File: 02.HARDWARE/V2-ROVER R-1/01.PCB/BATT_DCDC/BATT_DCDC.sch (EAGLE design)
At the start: 61 parts, among them J1 DF40C-20DP-0.4V_51_, K1 FLEX11, Q1 NVTFS9D6P04M8LTAG, Q2 2N7002PW, Q5 2N7002PW, U1 MCP6071T-E/OT, U3 TPS55330RTET, U7 MCP6071T-E/OT

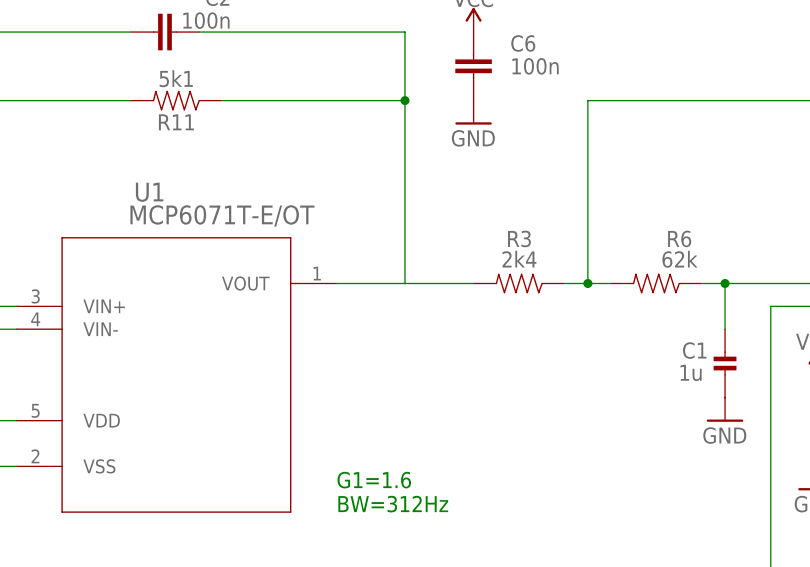
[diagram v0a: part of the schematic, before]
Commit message: Cierra el issue #65
Algunos cambios menores de rutado
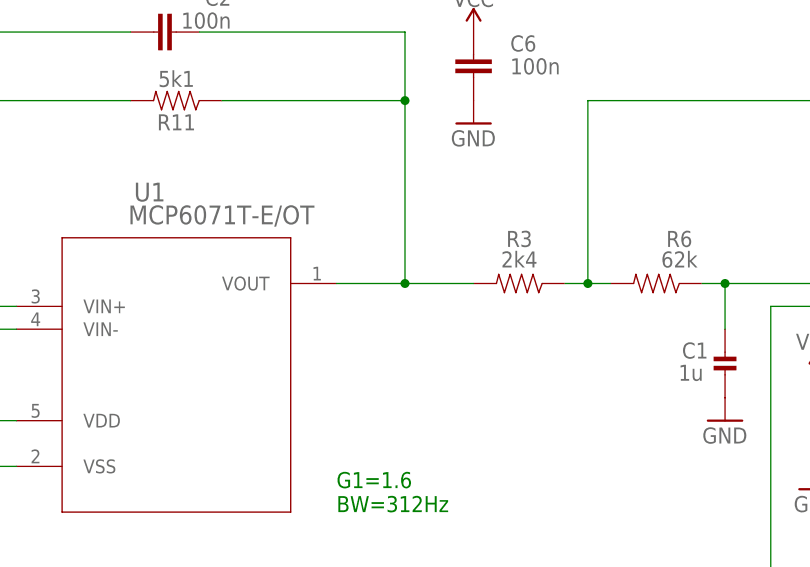
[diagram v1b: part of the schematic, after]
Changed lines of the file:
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@@
 <pinref part="R3" gate="G$1" pin="2"/>
 <wire x1="104.14" y1="71.12" x2="96.52" y2="71.12" width="0.1524" layer="91"/>
+<junction x="96.52" y="71.12"/>
 </segment>
 </net>

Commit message: Issue #72
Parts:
- removed Q5: 2N7002PW, SparkFun-DiscreteSemi:MOSFET-NCHANNEL2N7002PW
- removed R15: 100k, SparkFun-Resistors:RESISTOR0402
- added U2: LM5114BMF_NOPB, LM5114BMF_NOPB:LM5114BMF_NOPB
- R16: value 100k -> 10k
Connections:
- removed net N$8: Q1.G, Q5.D, R15.1
- new net N$9: Q1.G, U2.N_OUT, U2.P_OUT
- net GND: now also U2.VSS; no longer Q5.S
- net OP_SWITCH: now also U2.INB; no longer Q5.G
- net VSOURCE: now also U2.VDD; no longer R15.2
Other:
- moved on the sheet: R16
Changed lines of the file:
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@@
 <part name="GND58" library="SparkFun" deviceset="GND" device=""/>
 <part name="Q1" library="SamacSys_Parts" deviceset="NVTFS9D6P04M8LTAG" device=""/>
-<part name="R15" library="SparkFun-Resistors" library_urn="urn:adsk.eagle:library:532" deviceset="RESISTOR" device="0402" package3d_urn="urn:adsk.eagle:package:39657/1" value="100k"/>
-<part name="R16" library="SparkFun-Resistors" library_urn="urn:adsk.eagle:library:532" deviceset="RESISTOR" device="0402" package3d_urn="urn:adsk.eagle:package:39657/1" value="100k"/>
-<part name="Q5" library="SparkFun-DiscreteSemi" deviceset="MOSFET-NCHANNEL" device="2N7002PW" value="2N7002PW"/>
+<part name="R16" library="SparkFun-Resistors" library_urn="urn:adsk.eagle:library:532" deviceset="RESISTOR" device="0402" package3d_urn="urn:adsk.eagle:package:39657/1" value="10k"/>
 <part name="GND1" library="SparkFun" deviceset="GND" device=""/>
-<part name="GND2" library="SparkFun" deviceset="GND" device=""/>
 <part name="U1" library="MCP6071" deviceset="MCP6071T-E/OT" device=""/>
 <part name="R11" library="SparkFun-Resistors" library_urn="urn:adsk.eagle:library:532" deviceset="RESISTOR" device="0402" package3d_urn="urn:adsk.eagle:package:39657/1" value="5k1"/>
@@
 <part name="C9" library="SparkFun-Capacitors" deviceset="0.1UF" device="-0603-25V-(+80/-20%)" value="N.A."/>
 <part name="RSNS" library="SparkFun-Resistors" library_urn="urn:adsk.eagle:library:532" deviceset="RESISTOR" device="1206" package3d_urn="urn:adsk.eagle:package:39654/1" value="100mR"/>
+<part name="U2" library="LM5114BMF_NOPB" deviceset="LM5114BMF_NOPB" device=""/>
 </parts>
 <sheets>
@@
 <attribute name="VALUE" x="207.01" y="233.68" size="1.778" layer="96" align="center-left"/>
 </instance>
-<instance part="R15" gate="G$1" x="180.34" y="220.98" smashed="yes" rot="R180">
-<attribute name="NAME" x="180.34" y="219.456" size="1.778" layer="95" font="vector" rot="R180" align="bottom-center"/>
-<attribute name="VALUE" x="180.34" y="222.504" size="1.778" layer="96" font="vector" rot="R180" align="top-center"/>
-</instance>
-<instance part="R16" gate="G$1" x="203.2" y="185.42" smashed="yes" rot="R270">
-<attribute name="NAME" x="204.724" y="185.42" size="1.778" layer="95" font="vector" rot="R270" align="bottom-center"/>
-<attribute name="VALUE" x="201.676" y="185.42" size="1.778" layer="96" font="vector" rot="R270" align="top-center"/>
-</instance>
-<instance part="Q5" gate="G$1" x="187.96" y="193.04" smashed="yes" rot="MR0">
-<attribute name="NAME" x="193.04" y="200.66" size="1.778" layer="95" rot="MR0"/>
-<attribute name="VALUE" x="200.66" y="198.12" size="1.778" layer="96" rot="MR0"/>
-</instance>
-<instance part="GND1" gate="1" x="203.2" y="175.26" smashed="yes">
-<attribute name="VALUE" x="200.66" y="172.72" size="1.778" layer="96"/>
-</instance>
-<instance part="GND2" gate="1" x="187.96" y="175.26" smashed="yes">
-<attribute name="VALUE" x="185.42" y="172.72" size="1.778" layer="96"/>
+<instance part="R16" gate="G$1" x="220.98" y="185.42" smashed="yes" rot="R270">
+<attribute name="NAME" x="222.504" y="185.42" size="1.778" layer="95" font="vector" rot="R270" align="bottom-center"/>
+<attribute name="VALUE" x="219.456" y="185.42" size="1.778" layer="96" font="vector" rot="R270" align="top-center"/>
+</instance>
+<instance part="GND1" gate="1" x="220.98" y="175.26" smashed="yes">
+<attribute name="VALUE" x="218.44" y="172.72" size="1.778" layer="96"/>
 </instance>
 <instance part="U1" gate="A" x="50.8" y="68.58" smashed="yes">
@@
 <attribute name="NAME" x="22.86" y="61.976" size="1.778" layer="95" font="vector" rot="R180" align="bottom-center"/>
 <attribute name="VALUE" x="22.86" y="57.404" size="1.778" layer="96" font="vector" rot="R180" align="top-center"/>
+</instance>
+<instance part="U2" gate="G$1" x="182.88" y="195.58" smashed="yes" rot="MR180">
+<attribute name="NAME" x="189.23" y="190.5" size="1.778" layer="95" rot="MR180" align="center-left"/>
+<attribute name="VALUE" x="189.23" y="187.96" size="1.778" layer="96" rot="MR180" align="center-left"/>
 </instance>
 </instances>
@@
 <segment>
 <pinref part="R16" gate="G$1" pin="2"/>
-<wire x1="203.2" y1="180.34" x2="203.2" y2="177.8" width="0.1524" layer="91"/>
+<wire x1="220.98" y1="180.34" x2="220.98" y2="177.8" width="0.1524" layer="91"/>
 <pinref part="GND1" gate="1" pin="GND"/>
-</segment>
-<segment>
-<pinref part="Q5" gate="G$1" pin="S"/>
-<wire x1="187.96" y1="187.96" x2="187.96" y2="177.8" width="0.1524" layer="91"/>
-<pinref part="GND2" gate="1" pin="GND"/>
+<pinref part="U2" gate="G$1" pin="VSS"/>
+<wire x1="210.82" y1="200.66" x2="215.9" y2="200.66" width="0.1524" layer="91"/>
+<wire x1="215.9" y1="200.66" x2="215.9" y2="180.34" width="0.1524" layer="91"/>
+<wire x1="215.9" y1="180.34" x2="220.98" y2="180.34" width="0.1524" layer="91"/>
+<junction x="220.98" y="180.34"/>
 </segment>
 <segment>
@@
 <pinref part="Q1" gate="G$1" pin="S_1"/>
 <wire x1="170.18" y1="208.28" x2="170.18" y2="203.2" width="0.1524" layer="91"/>
-<wire x1="170.18" y1="228.6" x2="175.26" y2="228.6" width="0.1524" layer="91"/>
+<wire x1="170.18" y1="228.6" x2="172.72" y2="228.6" width="0.1524" layer="91"/>
 <junction x="170.18" y="228.6"/>
 <pinref part="Q1" gate="G$1" pin="S_2"/>
-<wire x1="175.26" y1="228.6" x2="193.04" y2="228.6" width="0.1524" layer="91"/>
+<wire x1="172.72" y1="228.6" x2="193.04" y2="228.6" width="0.1524" layer="91"/>
 <wire x1="193.04" y1="228.6" x2="198.12" y2="228.6" width="0.1524" layer="91"/>
 <wire x1="198.12" y1="226.06" x2="193.04" y2="226.06" width="0.1524" layer="91"/>
@@
 <wire x1="193.04" y1="223.52" x2="193.04" y2="226.06" width="0.1524" layer="91"/>
 <junction x="193.04" y="226.06"/>
-<pinref part="R15" gate="G$1" pin="2"/>
-<wire x1="175.26" y1="220.98" x2="175.26" y2="228.6" width="0.1524" layer="91"/>
-<junction x="175.26" y="228.6"/>
 <pinref part="C7" gate="G$1" pin="2"/>
 <wire x1="165.1" y1="203.2" x2="165.1" y2="208.28" width="0.1524" layer="91"/>
 <wire x1="170.18" y1="208.28" x2="165.1" y2="208.28" width="0.1524" layer="91"/>
 <junction x="170.18" y="208.28"/>
+<pinref part="U2" gate="G$1" pin="VDD"/>
+<wire x1="182.88" y1="195.58" x2="172.72" y2="195.58" width="0.1524" layer="91"/>
+<wire x1="172.72" y1="195.58" x2="172.72" y2="228.6" width="0.1524" layer="91"/>
+<junction x="172.72" y="228.6"/>
 </segment>
 </net>
@@
 </segment>
 </net>
-<net name="N$8" class="0">
-<segment>
-<pinref part="R15" gate="G$1" pin="1"/>
-<pinref part="Q1" gate="G$1" pin="G"/>
-<wire x1="185.42" y1="220.98" x2="187.96" y2="220.98" width="0.1524" layer="91"/>
-<pinref part="Q5" gate="G$1" pin="D"/>
-<wire x1="187.96" y1="220.98" x2="198.12" y2="220.98" width="0.1524" layer="91"/>
-<wire x1="187.96" y1="198.12" x2="187.96" y2="220.98" width="0.1524" layer="91"/>
-<junction x="187.96" y="220.98"/>
-</segment>
-</net>
 <net name="OP_SWITCH" class="0">
 <segment>
-<label x="208.28" y="193.04" size="1.778" layer="95"/>
-<pinref part="Q5" gate="G$1" pin="G"/>
-<wire x1="195.58" y1="193.04" x2="203.2" y2="193.04" width="0.1524" layer="91"/>
+<label x="226.06" y="198.12" size="1.778" layer="95"/>
 <pinref part="R16" gate="G$1" pin="1"/>
-<wire x1="203.2" y1="190.5" x2="203.2" y2="193.04" width="0.1524" layer="91"/>
-<junction x="203.2" y="193.04"/>
-<wire x1="241.3" y1="193.04" x2="203.2" y2="193.04" width="0.1524" layer="91"/>
-<label x="241.3" y="193.04" size="1.778" layer="95" xref="yes"/>
+<wire x1="220.98" y1="190.5" x2="220.98" y2="198.12" width="0.1524" layer="91"/>
+<wire x1="241.3" y1="198.12" x2="220.98" y2="198.12" width="0.1524" layer="91"/>
+<label x="241.3" y="198.12" size="1.778" layer="95" xref="yes"/>
+<pinref part="U2" gate="G$1" pin="INB"/>
+<wire x1="210.82" y1="198.12" x2="220.98" y2="198.12" width="0.1524" layer="91"/>
+<junction x="220.98" y="198.12"/>
 </segment>
 <segment>
@@
 </segment>
 </net>
+<net name="N$9" class="0">
+<segment>
+<pinref part="U2" gate="G$1" pin="P_OUT"/>
+<pinref part="U2" gate="G$1" pin="N_OUT"/>
+<wire x1="182.88" y1="198.12" x2="182.88" y2="200.66" width="0.1524" layer="91"/>
+<wire x1="182.88" y1="200.66" x2="180.34" y2="200.66" width="0.1524" layer="91"/>
+<wire x1="180.34" y1="200.66" x2="180.34" y2="220.98" width="0.1524" layer="91"/>
+<junction x="182.88" y="200.66"/>
+<pinref part="Q1" gate="G$1" pin="G"/>
+<wire x1="180.34" y1="220.98" x2="198.12" y2="220.98" width="0.1524" layer="91"/>
+</segment>
+</net>

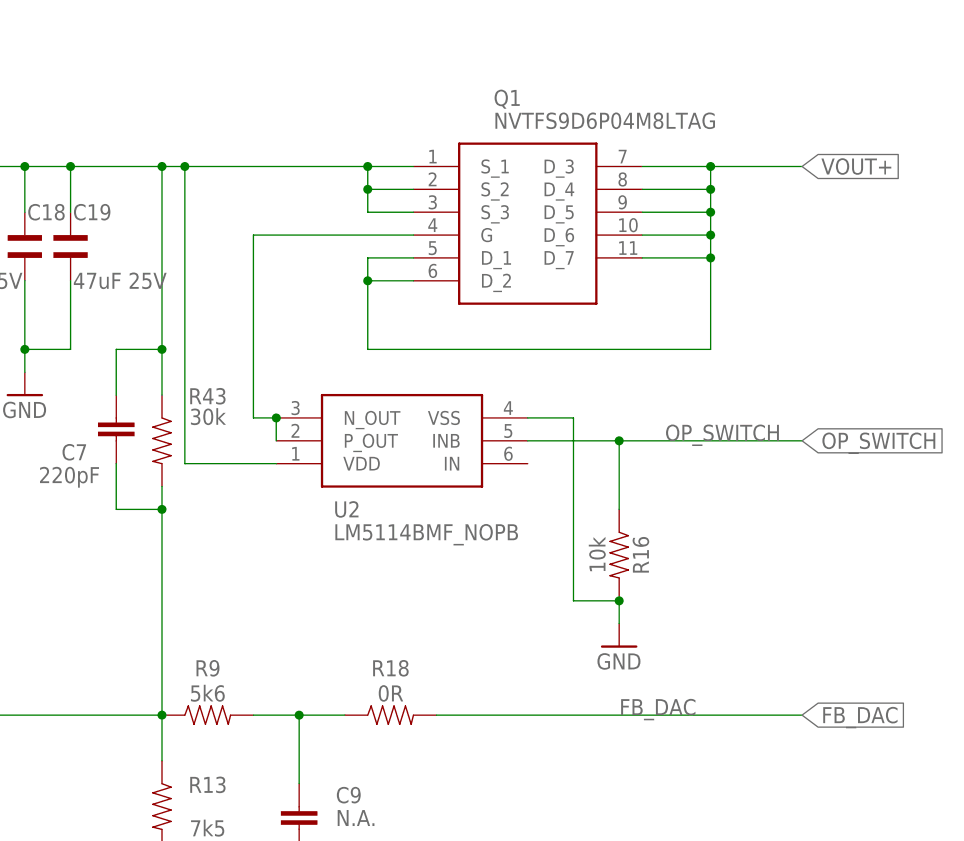
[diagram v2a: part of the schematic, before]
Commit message: Se corrige señal IN a VSOURCE para  que funcione como negador
Se mueven algunos componentes para  que no se solapen.
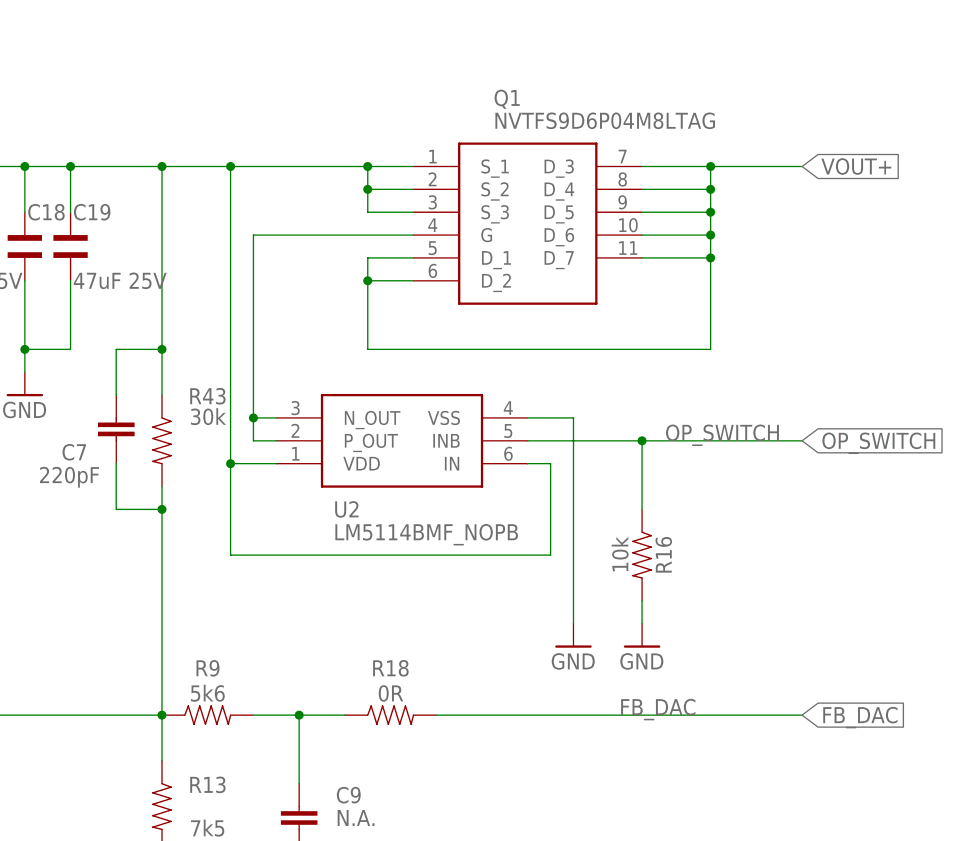
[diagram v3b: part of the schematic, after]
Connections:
- net VSOURCE: now also U2.IN
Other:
- moved on the sheet: R16
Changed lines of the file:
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@@
 <part name="RSNS" library="SparkFun-Resistors" library_urn="urn:adsk.eagle:library:532" deviceset="RESISTOR" device="1206" package3d_urn="urn:adsk.eagle:package:39654/1" value="100mR"/>
 <part name="U2" library="LM5114BMF_NOPB" deviceset="LM5114BMF_NOPB" device=""/>
+<part name="GND2" library="SparkFun" deviceset="GND" device=""/>
 </parts>
 <sheets>
@@
 <attribute name="VALUE" x="207.01" y="233.68" size="1.778" layer="96" align="center-left"/>
 </instance>
-<instance part="R16" gate="G$1" x="220.98" y="185.42" smashed="yes" rot="R270">
-<attribute name="NAME" x="222.504" y="185.42" size="1.778" layer="95" font="vector" rot="R270" align="bottom-center"/>
-<attribute name="VALUE" x="219.456" y="185.42" size="1.778" layer="96" font="vector" rot="R270" align="top-center"/>
-</instance>
-<instance part="GND1" gate="1" x="220.98" y="175.26" smashed="yes">
-<attribute name="VALUE" x="218.44" y="172.72" size="1.778" layer="96"/>
+<instance part="R16" gate="G$1" x="223.52" y="185.42" smashed="yes" rot="R270">
+<attribute name="NAME" x="225.044" y="185.42" size="1.778" layer="95" font="vector" rot="R270" align="bottom-center"/>
+<attribute name="VALUE" x="221.996" y="185.42" size="1.778" layer="96" font="vector" rot="R270" align="top-center"/>
+</instance>
+<instance part="GND1" gate="1" x="223.52" y="175.26" smashed="yes">
+<attribute name="VALUE" x="220.98" y="172.72" size="1.778" layer="96"/>
 </instance>
 <instance part="U1" gate="A" x="50.8" y="68.58" smashed="yes">
@@
 <attribute name="NAME" x="189.23" y="190.5" size="1.778" layer="95" rot="MR180" align="center-left"/>
 <attribute name="VALUE" x="189.23" y="187.96" size="1.778" layer="96" rot="MR180" align="center-left"/>
+</instance>
+<instance part="GND2" gate="1" x="215.9" y="175.26" smashed="yes">
+<attribute name="VALUE" x="213.36" y="172.72" size="1.778" layer="96"/>
 </instance>
 </instances>
@@
 <segment>
 <pinref part="R16" gate="G$1" pin="2"/>
-<wire x1="220.98" y1="180.34" x2="220.98" y2="177.8" width="0.1524" layer="91"/>
+<wire x1="223.52" y1="180.34" x2="223.52" y2="177.8" width="0.1524" layer="91"/>
 <pinref part="GND1" gate="1" pin="GND"/>
+</segment>
+<segment>
 <pinref part="U2" gate="G$1" pin="VSS"/>
 <wire x1="210.82" y1="200.66" x2="215.9" y2="200.66" width="0.1524" layer="91"/>
-<wire x1="215.9" y1="200.66" x2="215.9" y2="180.34" width="0.1524" layer="91"/>
-<wire x1="215.9" y1="180.34" x2="220.98" y2="180.34" width="0.1524" layer="91"/>
-<junction x="220.98" y="180.34"/>
+<wire x1="215.9" y1="200.66" x2="215.9" y2="177.8" width="0.1524" layer="91"/>
+<pinref part="GND2" gate="1" pin="GND"/>
 </segment>
 <segment>
@@
 <pinref part="Q1" gate="G$1" pin="S_1"/>
 <wire x1="170.18" y1="208.28" x2="170.18" y2="203.2" width="0.1524" layer="91"/>
-<wire x1="170.18" y1="228.6" x2="172.72" y2="228.6" width="0.1524" layer="91"/>
+<wire x1="170.18" y1="228.6" x2="177.8" y2="228.6" width="0.1524" layer="91"/>
 <junction x="170.18" y="228.6"/>
 <pinref part="Q1" gate="G$1" pin="S_2"/>
-<wire x1="172.72" y1="228.6" x2="193.04" y2="228.6" width="0.1524" layer="91"/>
+<wire x1="177.8" y1="228.6" x2="193.04" y2="228.6" width="0.1524" layer="91"/>
 <wire x1="193.04" y1="228.6" x2="198.12" y2="228.6" width="0.1524" layer="91"/>
 <wire x1="198.12" y1="226.06" x2="193.04" y2="226.06" width="0.1524" layer="91"/>
@@
 <junction x="170.18" y="208.28"/>
 <pinref part="U2" gate="G$1" pin="VDD"/>
-<wire x1="182.88" y1="195.58" x2="172.72" y2="195.58" width="0.1524" layer="91"/>
-<wire x1="172.72" y1="195.58" x2="172.72" y2="228.6" width="0.1524" layer="91"/>
-<junction x="172.72" y="228.6"/>
+<wire x1="182.88" y1="195.58" x2="177.8" y2="195.58" width="0.1524" layer="91"/>
+<wire x1="177.8" y1="195.58" x2="177.8" y2="228.6" width="0.1524" layer="91"/>
+<junction x="177.8" y="228.6"/>
+<wire x1="177.8" y1="195.58" x2="177.8" y2="185.42" width="0.1524" layer="91"/>
+<wire x1="177.8" y1="185.42" x2="213.36" y2="185.42" width="0.1524" layer="91"/>
+<wire x1="213.36" y1="185.42" x2="213.36" y2="195.58" width="0.1524" layer="91"/>
+<pinref part="U2" gate="G$1" pin="IN"/>
+<wire x1="213.36" y1="195.58" x2="210.82" y2="195.58" width="0.1524" layer="91"/>
+<junction x="177.8" y="195.58"/>
 </segment>
 </net>
@@
 <label x="226.06" y="198.12" size="1.778" layer="95"/>
 <pinref part="R16" gate="G$1" pin="1"/>
-<wire x1="220.98" y1="190.5" x2="220.98" y2="198.12" width="0.1524" layer="91"/>
-<wire x1="241.3" y1="198.12" x2="220.98" y2="198.12" width="0.1524" layer="91"/>
+<wire x1="223.52" y1="190.5" x2="223.52" y2="198.12" width="0.1524" layer="91"/>
+<wire x1="241.3" y1="198.12" x2="223.52" y2="198.12" width="0.1524" layer="91"/>
 <label x="241.3" y="198.12" size="1.778" layer="95" xref="yes"/>
 <pinref part="U2" gate="G$1" pin="INB"/>
-<wire x1="210.82" y1="198.12" x2="220.98" y2="198.12" width="0.1524" layer="91"/>
-<junction x="220.98" y="198.12"/>
+<wire x1="210.82" y1="198.12" x2="223.52" y2="198.12" width="0.1524" layer="91"/>
+<junction x="223.52" y="198.12"/>
 </segment>
 <segment>
@@
 <pinref part="U2" gate="G$1" pin="P_OUT"/>
 <pinref part="U2" gate="G$1" pin="N_OUT"/>
-<wire x1="182.88" y1="198.12" x2="182.88" y2="200.66" width="0.1524" layer="91"/>
 <wire x1="182.88" y1="200.66" x2="180.34" y2="200.66" width="0.1524" layer="91"/>
 <wire x1="180.34" y1="200.66" x2="180.34" y2="220.98" width="0.1524" layer="91"/>
-<junction x="182.88" y="200.66"/>
 <pinref part="Q1" gate="G$1" pin="G"/>
 <wire x1="180.34" y1="220.98" x2="198.12" y2="220.98" width="0.1524" layer="91"/>
-</segment>
-</net>
+<wire x1="180.34" y1="200.66" x2="180.34" y2="198.12" width="0.1524" layer="91"/>
+<junction x="180.34" y="200.66"/>
+<wire x1="180.34" y1="198.12" x2="182.88" y2="198.12" width="0.1524" layer="91"/>
+</segment>
+</net>

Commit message: Revision antes de envio SETI 3ra produccion - SEP-23
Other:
- note added: "STEP UP DCDC CONVERTER ROVER R-1- SEP2023 - v3 (3ra producion)"
- note removed: "STEP UP DCDC CONVERTER ROVER1K - DEC'22-v2"
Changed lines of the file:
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@@
 <text x="17.78" y="116.84" size="5.08" layer="94">IOSENSE LOWPASS FILTERING</text>
 <text x="35.56" y="241.3" size="5.08" layer="94">STEP UP DCDC CONVERTER
-ROVER1K - DEC'22-v2</text>
+ROVER R-1- SEP2023 - v3 (3ra producion)</text>
 <text x="88.9" y="45.72" size="1.778" layer="91">G1=1.6
 BW=312Hz</text>
